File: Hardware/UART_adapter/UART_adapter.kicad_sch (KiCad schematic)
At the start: 2 parts, among them J1 Conn_02x07_Top_Bottom

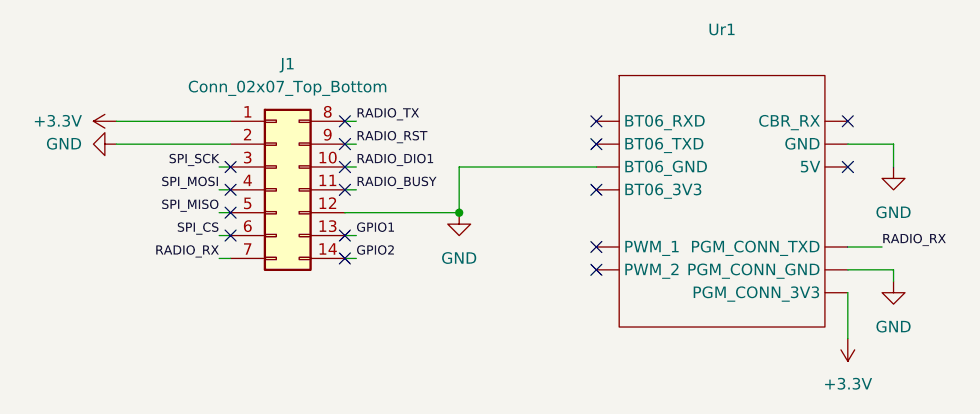
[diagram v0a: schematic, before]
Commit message: Fixed USB traces, radio connectors, finished UART adapter
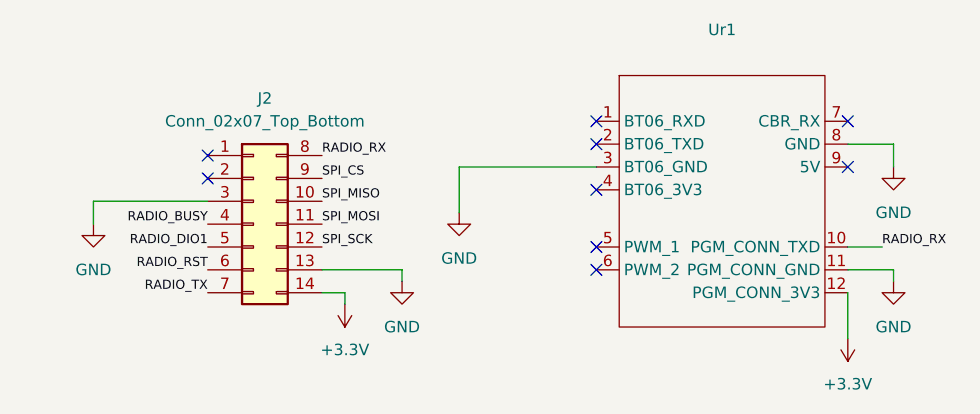
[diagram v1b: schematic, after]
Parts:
- removed J1: Conn_02x07_Top_Bottom, Connector_PinHeader_2.54mm:PinHeader_2x07_P2.54mm_Horizontal, symbol Connector_Generic:Conn_02x07_Top_Bottom
- added J2: Conn_02x07_Top_Bottom, Connector_PinHeader_2.54mm:PinHeader_2x07_P2.54mm_Horizontal, symbol Connector_Generic:Conn_02x07_Top_Bottom
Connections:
- net +3.3V: now also Ur1.12 (PGM_CONN_3V3), J2.14 (Pin_14); no longer Ur1. (PGM_CONN_3V3)
- net GND: now also Ur1.11 (PGM_CONN_GND), Ur1.3 (BT06_GND), Ur1.8 (GND), J2.13 (Pin_13), J2.3 (Pin_3); no longer Ur1. (PGM_CONN_3V3)
- net RADIO_BUSY: now also J2.4 (Pin_4)
- net RADIO_DIO1: now also J2.5 (Pin_5)
- net RADIO_RST: now also J2.6 (Pin_6)
- net RADIO_RX: now also Ur1.10 (PGM_CONN_TXD), J2.8 (Pin_8); no longer Ur1. (PGM_CONN_3V3)
- net RADIO_TX: now also J2.7 (Pin_7)
- net SPI_CS: now also J2.9 (Pin_9)
- net SPI_MISO: now also J2.10 (Pin_10)
- net SPI_MOSI: now also J2.11 (Pin_11)
- net SPI_SCK: now also J2.12 (Pin_12)
- no-connect marks 17 -> 9

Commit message: Updated eggfinder to correct wiring
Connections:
- net +3.3V: now also Ur1.9 (5V); no longer Ur1.12 (PGM_CONN_3V3)
- net RADIO_RX: now also Ur1.7 (CBR_RX); no longer Ur1.10 (PGM_CONN_TXD)
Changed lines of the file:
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@@
+	)
+	(no_connect
+		(at 160.02 106.68)
+	)
+	(no_connect
+		(at 160.02 101.6)
 	)
 	(no_connect
@@
 	)
 	(no_connect
-		(at 160.02 92.71)
-	)
-	(no_connect
 		(at 132.08 87.63)
 	)
@@
 		(at 132.08 101.6)
 	)
-	(no_connect
-		(at 160.02 87.63)
-	)
 	(wire
 		(pts
@@
 		(pts
 			(xy 104.14 107.95) (xy 104.14 106.68)
-		)
-		(stroke
-			(width 0)
-			(type default)
-		)
-	)
-	(wire
-		(pts
-			(xy 160.02 101.6) (xy 163.83 101.6)
-		)
-		(stroke
-			(width 0)
-			(type default)
-		)
-	)
-	(wire
-		(pts
-			(xy 160.02 106.68) (xy 160.02 111.76)
 		)
 		(stroke
@@
 		)
 	)
-	(label "RADIO_RX"
-		(at 163.83 101.6 0)
-		(effects
-			(font
-				(size 1.016 1.016)
-			)
-			(justify left bottom)
-		)
-	)
 	(label "SPI_CS"
 		(at 101.6 93.98 0)
@@
 		)
 	)
+	(label "RADIO_RX"
+		(at 160.02 87.63 0)
+		(effects
+			(font
+				(size 1.016 1.016)
+			)
+			(justify left bottom)
+		)
+	)
 	(label "SPI_MISO"
 		(at 101.6 96.52 0)
@@
 	(symbol
 		(lib_id "power:+3.3V")
-		(at 160.02 111.76 180)
+		(at 160.02 92.71 180)
 		(unit 1)
 		(exclude_from_sim no)
@@
 		(fields_autoplaced yes)
 		(property "Reference" "#PWR07"
-			(at 160.02 107.95 0)
+			(at 160.02 88.9 0)
 			(effects
 				(font
@@
 		)
 		(property "Value" "+3.3V"
-			(at 160.02 116.84 0)
+			(at 160.02 97.79 0)
 			(effects
 				(font
@@
 		)
 		(property "Footprint" ""
-			(at 160.02 111.76 0)
+			(at 160.02 92.71 0)
 			(effects
 				(font
@@
 		)
 		(property "Datasheet" ""
-			(at 160.02 111.76 0)
+			(at 160.02 92.71 0)
 			(effects
 				(font
@@
 		)
 		(property "Description" "Power symbol creates a global label with name \"+3.3V\""
-			(at 160.02 111.76 0)
-			(effects
-				(font
+			(at 160.02 92.71 0)
+			(effects
+				(font
